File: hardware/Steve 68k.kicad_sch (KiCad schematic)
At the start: 52 parts, among them IC1 MC68008FN8, J1 Conn_02x32_Odd_Even, J2 Serial 1, J3 Serial 2, J4 CLK Select, J5 I2C, SW1 Reset, U1 74LS32, U10 74HC04, U2 28C256, U3 GAL16V8, U4 74HC04, U5 MC68681FN, U6 74HC04, U7 AS6C4008-55PCN, U8 Max705, U9 PCA9564, X1 CXO_DIP8, X2 1.8432 Mhz

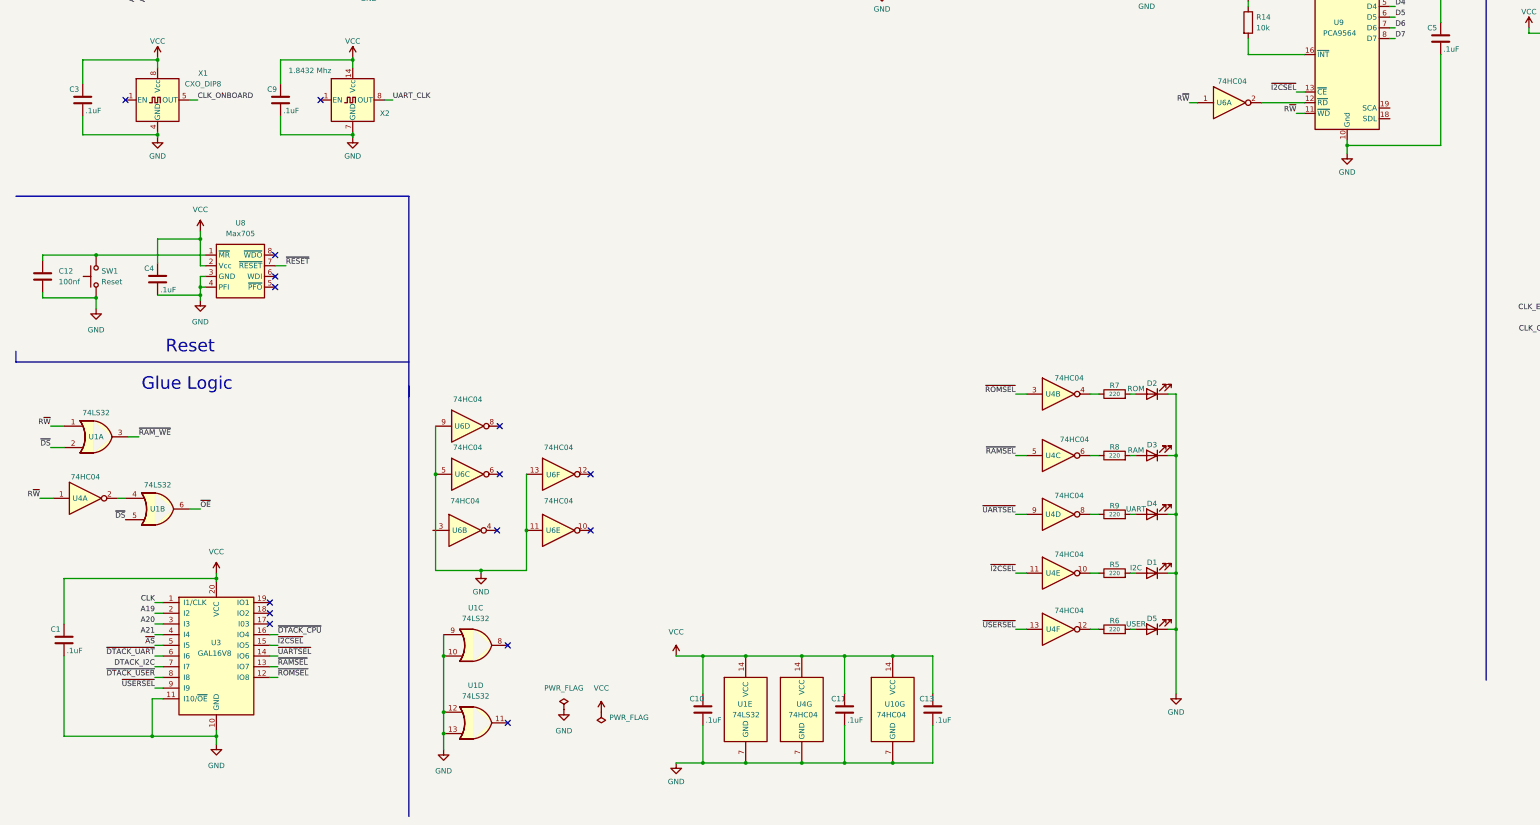
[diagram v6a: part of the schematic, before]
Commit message: Added a second GAL
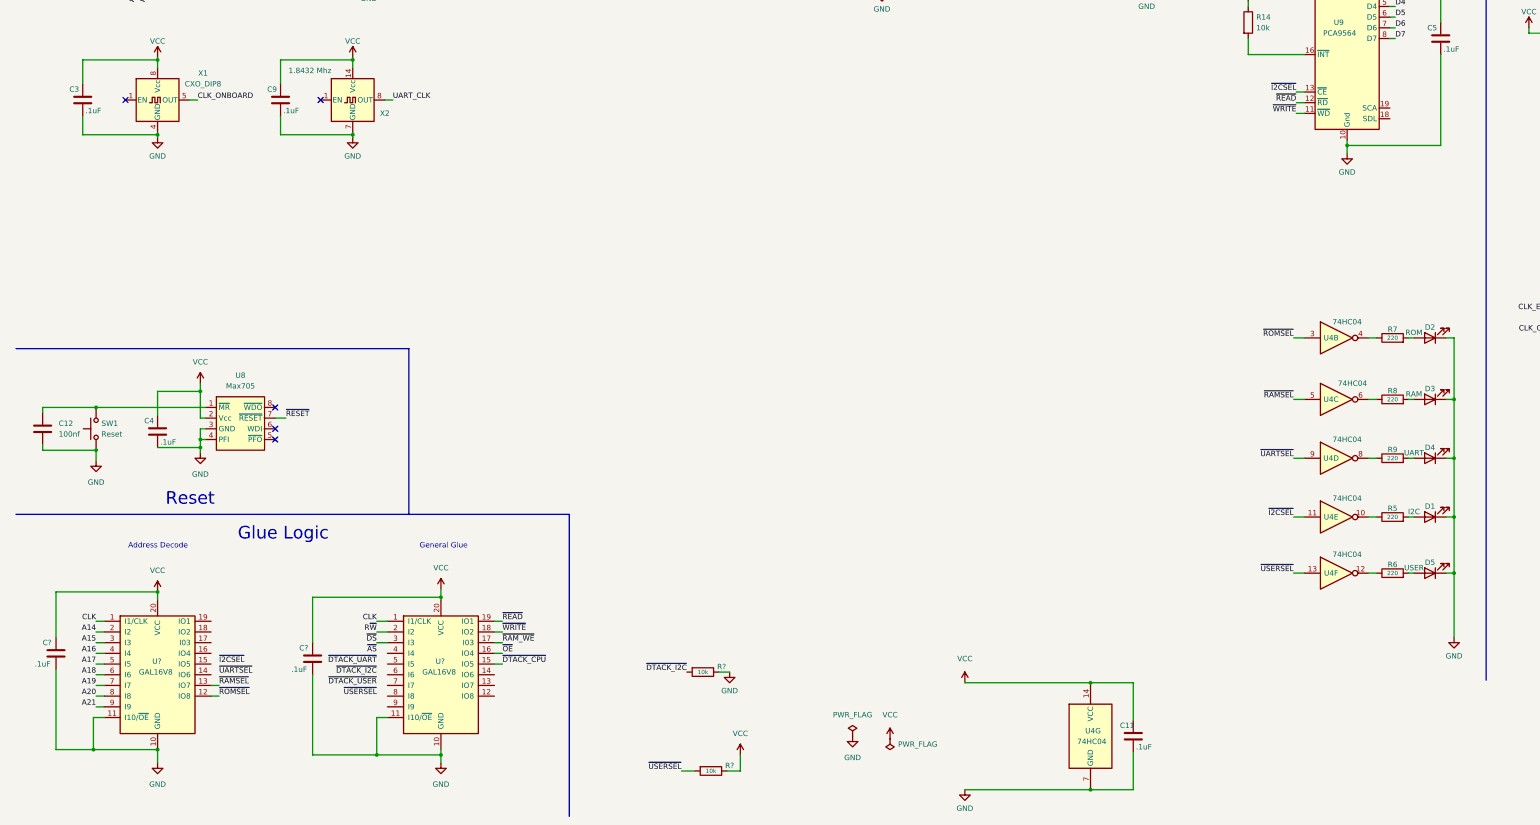
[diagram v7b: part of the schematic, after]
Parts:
- removed C1, C10, C13: .1uF, Capacitor_SMD:C_0603_1608Metric, symbol Device:C
- removed U1: 74LS32, Package_SO:SOIC-14_3.9x8.7mm_P1.27mm, symbol 74xx:74LS32
- removed U10, U6: 74HC04, symbol 74xx:74HC04
- removed U3: GAL16V8, Package_DIP:DIP-20_W7.62mm_Socket_LongPads, symbol Logic_Programmable:GAL16V8
- removed unit 1 of U4
- added C? (x2): .1uF, Capacitor_SMD:C_0603_1608Metric, symbol Device:C
- added R? (x2): 10k, Resistor_SMD:R_0603_1608Metric, symbol Device:R
- added U? (x2): GAL16V8, Package_DIP:DIP-20_W7.62mm_Socket_LongPads, symbol Logic_Programmable:GAL16V8
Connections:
- net A14: now also U?.2 (I2)
- net A15: now also U?.3 (I3)
- net A16: now also U?.4 (I4)
- net A17: now also U?.5 (I5)
- net A18: now also U?.6 (I6)
- net A19: now also U?.7 (I7)
- net A20: now also U?.8 (I8)
- net A21: now also U?.9 (I9)
- net CLK: now also U?.1 (I1/CLK), U?.1 (I1/CLK)
- net GND: now also C?.2, C?.2, R?.1, U?.10 (GND), U?.10 (GND), U?.11 (I10/~{OE}), U?.11 (I10/~{OE})
- net R~{W}: now also U?.2 (I2); no longer U9.11 (~{WD})
- net VCC: now also C?.1, C?.1, R?.1, U?.20 (VCC), U?.20 (VCC)
- net ~{DS}: now also U?.3 (I3)
- net ~{DTACK_CPU}: now also U?.15 (IO5)
- net ~{OE}: now also U?.16 (IO4)
- net ~{RAMSEL}: now also U?.13 (IO7)
- net ~{RAM_WE}: now also U?.17 (I03)
- net ~{ROMSEL}: now also U?.12 (IO8)
- net ~{USERSEL}: now also R?.2
- net ~{READ}: now reaches U9.12 (~{RD})
- net ~{READ}: now also U?.19 (IO1)
- new net ~{DTACK_I2C}: R?.2
- new net ~{WRITE}: U9.11 (~{WD}), U?.18 (IO2)
- no-connect marks 23 -> 13
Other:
- note added: "Address Decode"
- note added: "General Glue"
- moved on the sheet: C11, C12, C4, D1, D2, D3, D4, D5, R5, R6, R7, R8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
